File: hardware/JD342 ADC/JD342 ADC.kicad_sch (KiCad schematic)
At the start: 12 parts, among them U1 ADS7279IPW, U2 OPA192IDBVR

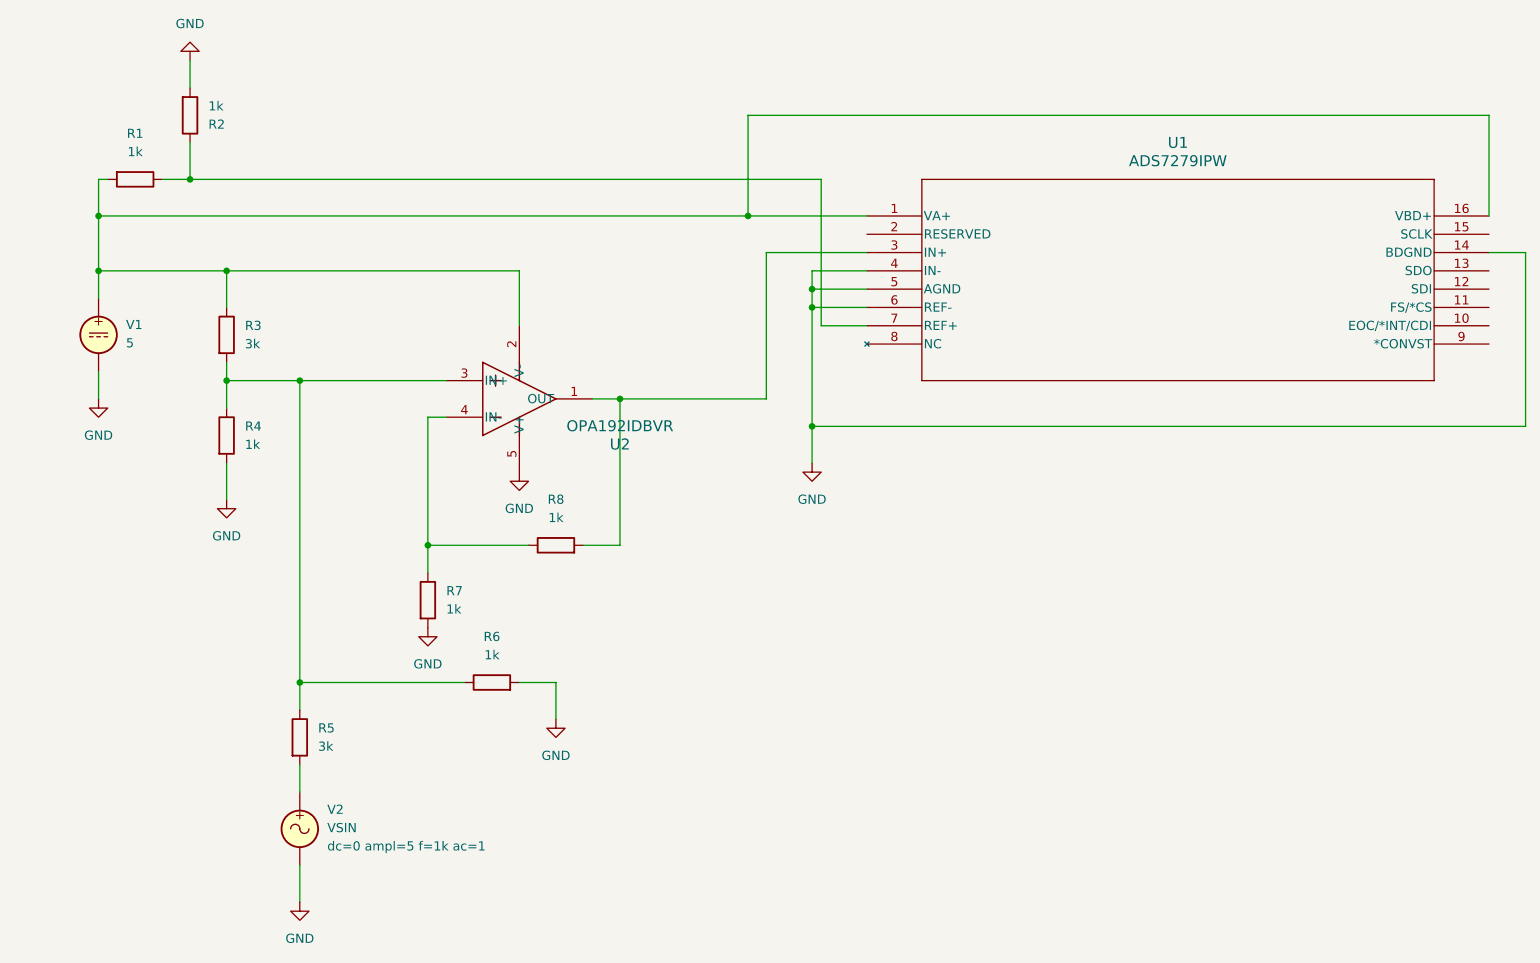
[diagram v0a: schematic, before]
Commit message: feat: opAmpCircuit cleanup
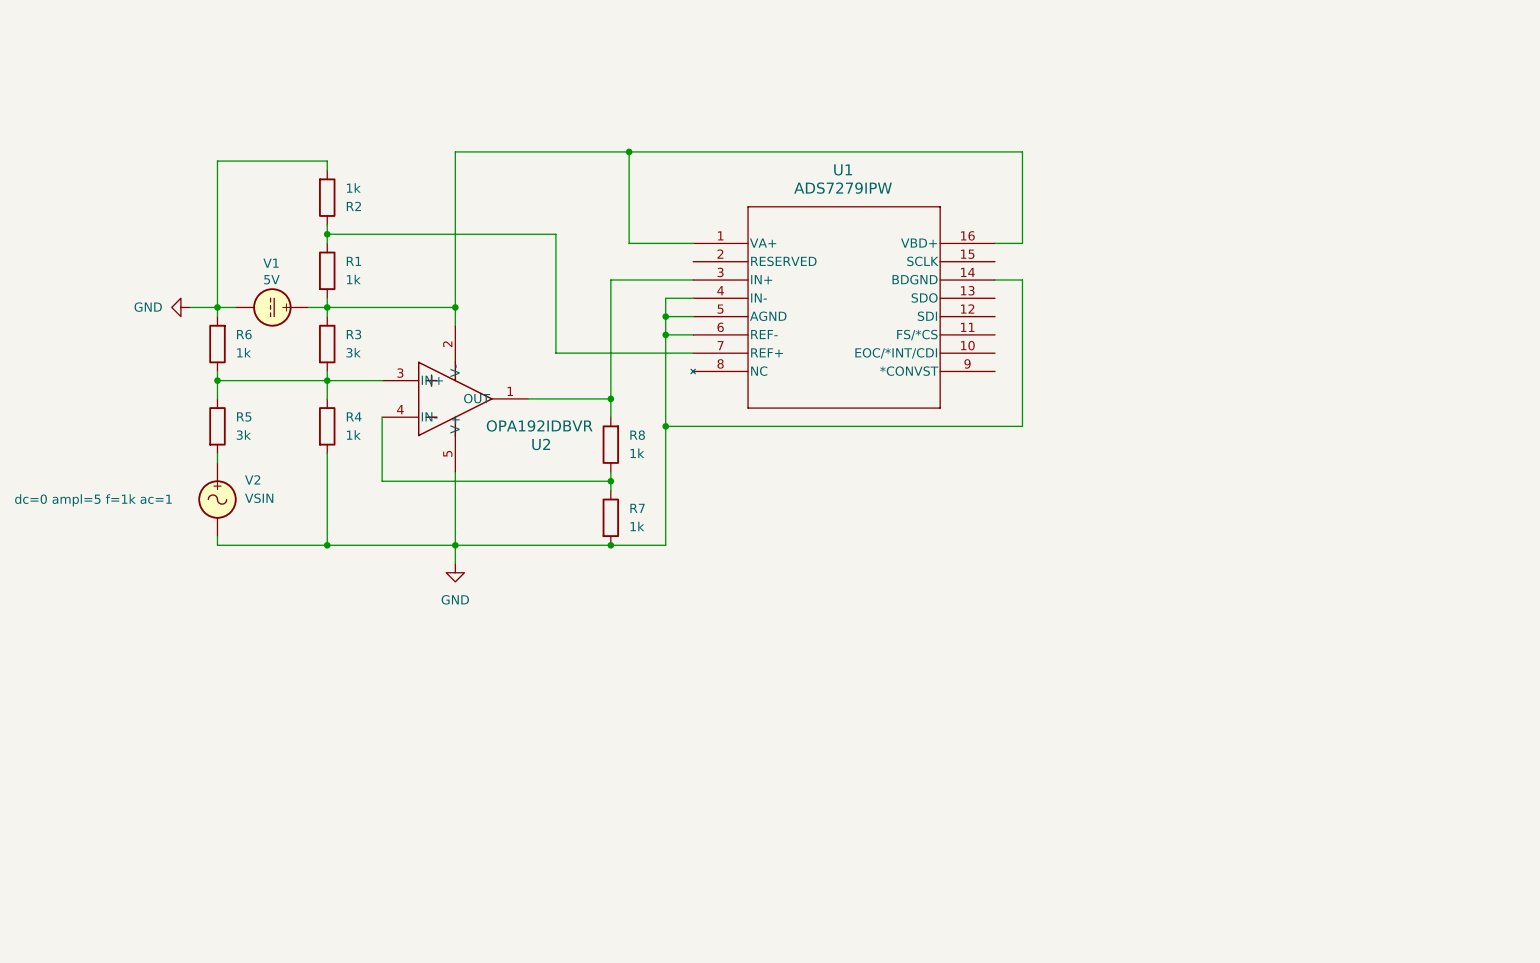
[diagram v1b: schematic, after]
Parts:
- V1: value 5 -> 5V
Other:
- moved on the sheet: R1, R2, R3, R4, R5, R7, U1, U2, V1, V2
